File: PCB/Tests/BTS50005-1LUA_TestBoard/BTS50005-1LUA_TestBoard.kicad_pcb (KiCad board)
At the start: 2 copper layers, 48.3 x 21.6 mm, 16 parts, among them J1 Conn_01x06, Q1 BTS500101LUAAUMA1

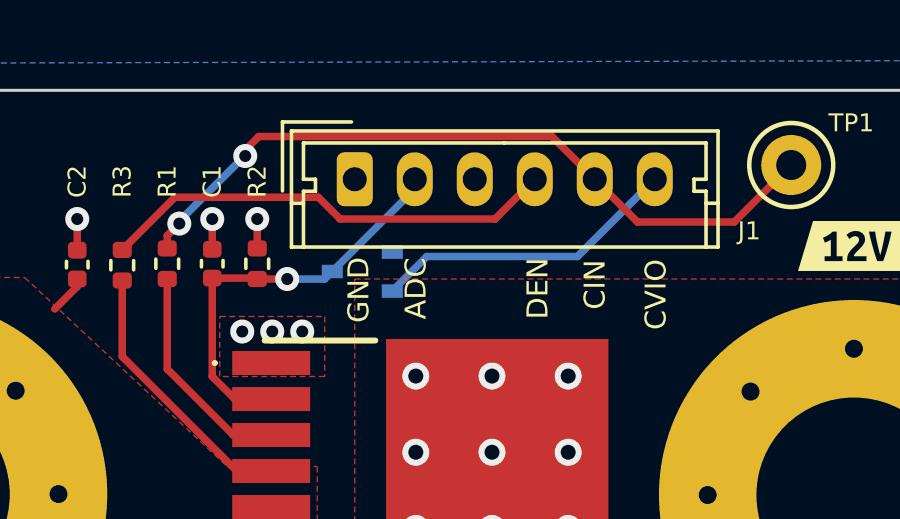
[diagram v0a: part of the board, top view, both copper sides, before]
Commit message: Added NTC for evaluation board
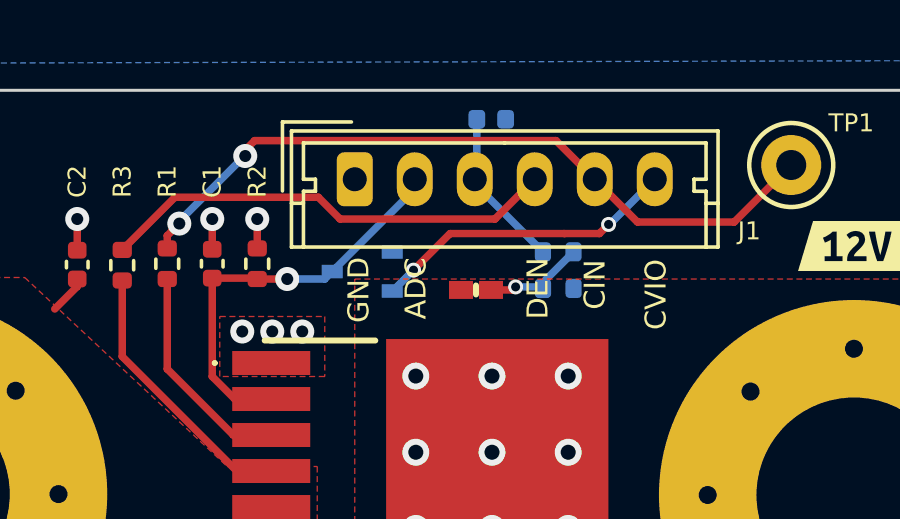
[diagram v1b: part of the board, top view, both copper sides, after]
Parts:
- added C4: 100nF, Capacitor_SMD:C_0402_1005Metric, B.Cu at (123.8, 30.2)
- added R4: 4k7, Resistor_SMD:R_0402_1005Metric, B.Cu at (126.0, 34.6)
- added R5: 75, Resistor_SMD:R_0402_1005Metric, B.Cu at (126.0, 35.8)
- added RT1: B57232V5103F360, PDM_Additional:THRMC1005X60N, F.Cu at (123.3, 35.9)
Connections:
- J1 pad 3: unconnected-(J1-Pad3) -> CONTROLLER_TEMP
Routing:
- net CONTROLLER_TEMP: track 0.00 -> 5.54 mm
- net Net-(R4-Pad1): track 0.00 -> 3.44 mm, vias 0 -> 1
- net CONTOLLER_VDD: vias 0 -> 2
